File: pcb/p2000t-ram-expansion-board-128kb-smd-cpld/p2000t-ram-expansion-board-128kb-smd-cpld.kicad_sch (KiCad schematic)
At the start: 12 parts, among them J1 EXPANSION BOARD, J2 POWER, J3 TERMINAL, U1 ATF1502ASV-xAx44, U2 62128

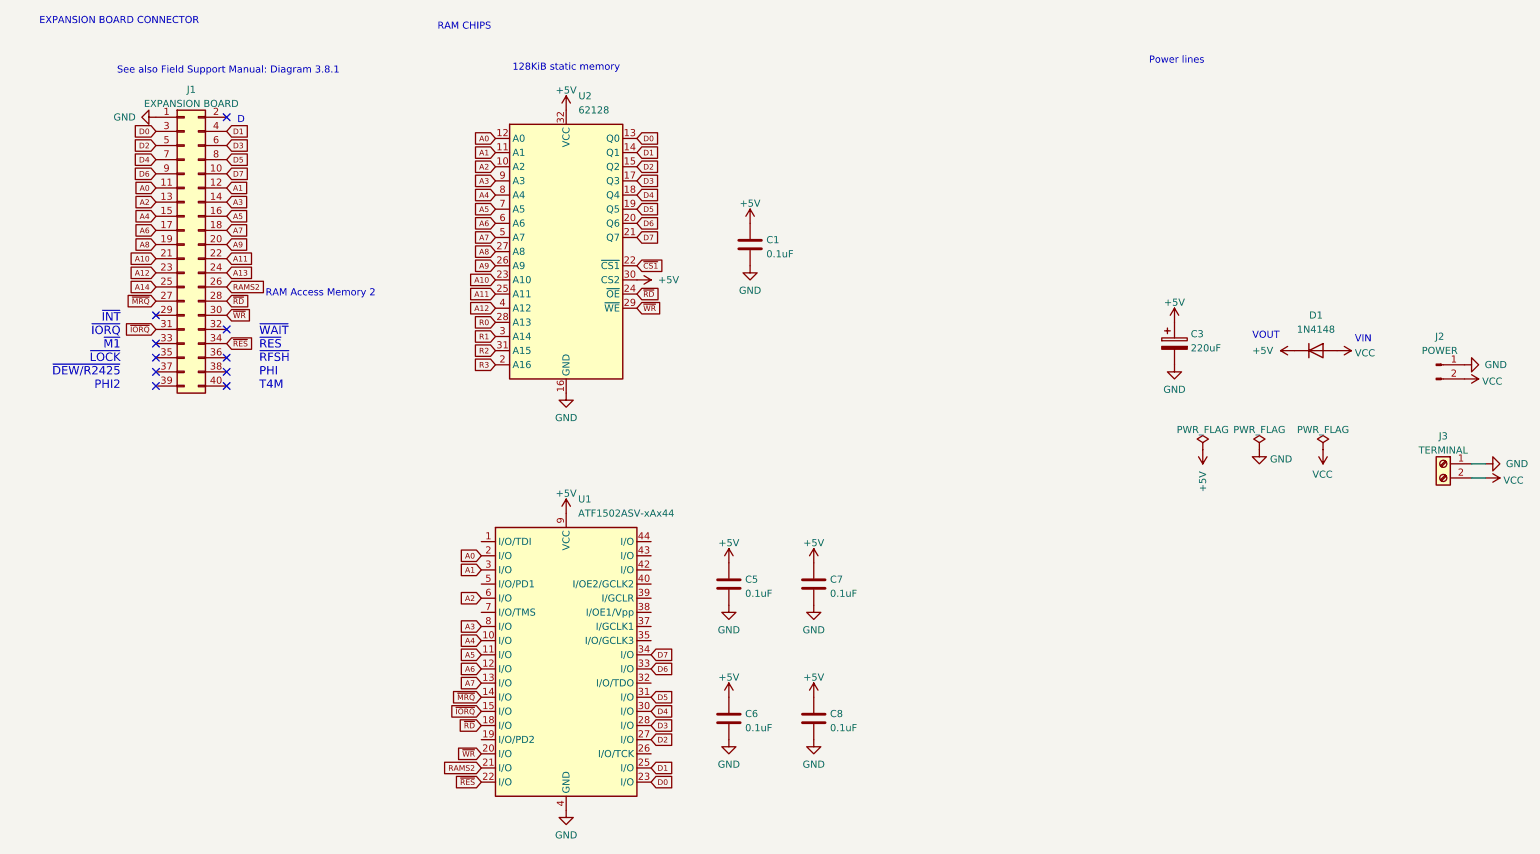
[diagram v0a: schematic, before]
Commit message: Initial commit CPLD-based RAM expansion
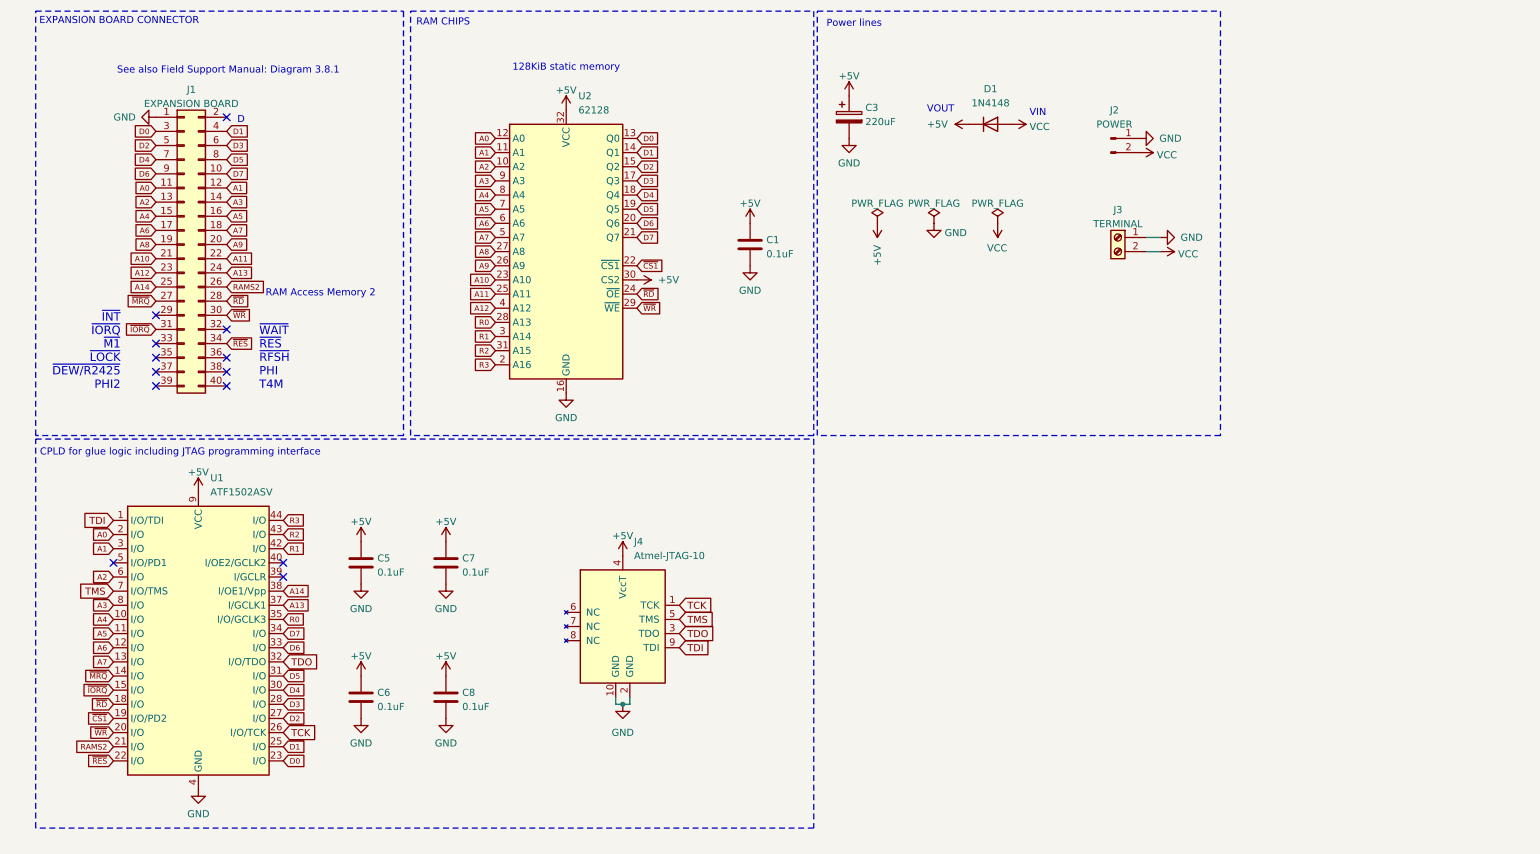
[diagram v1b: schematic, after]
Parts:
- added J4: Atmel-JTAG-10, Connector_IDC:IDC-Header_2x05_P2.54mm_Vertical, symbol atf1504_plcc44_breakout:Atmel-JTAG-10
- U1: value ATF1502ASV-xAx44 -> ATF1502ASV
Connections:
- net +5V: now also J4.4 (VccT)
- net A13: now also U1.37 (I/GCLK1)
- net A14: now also U1.38 (I/OE1/Vpp)
- net GND: now also J4.10 (GND), J4.2 (GND)
- net R0: now also U1.35 (I/O/GCLK3)
- net R1: now also U1.42 (I/O)
- net R2: now also U1.43 (I/O)
- net R3: now also U1.44 (I/O)
- net ~{CS1}: now also U1.19 (I/O/PD2)
- net TDI: now reaches U1.1 (I/O/TDI)
- net TDI: now also J4.9 (TDI)
- net TCK: now reaches U1.26 (I/O/TCK)
- net TCK: now also J4.1 (TCK)
- net TDO: now reaches U1.32 (I/O/TDO)
- net TDO: now also J4.3 (TDO)
- net TMS: now reaches U1.7 (I/O/TMS)
- net TMS: now also J4.5 (TMS)
- no-connect marks 10 -> 13
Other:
- note added: "CPLD for glue logic including JTAG programming interface"
- title: Philips P2000T 128KiB memory expansion board (SMD) -> Philips P2000T 128KiB memory expansion board (SMD / CPLD)
- moved on the sheet: C3, C5, C6, C7, C8, D1, J2, J3, U1
